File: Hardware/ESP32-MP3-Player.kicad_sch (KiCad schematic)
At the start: 17 parts, among them J1 Micro_SD_Card, J2 AudioJack3, J3 Battery, SW1 Reset, U1 ESP32-WROOM-32E, U2 MAX98357A, U3 AMS1117-3.3

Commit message: hardware: new analog circuit design
The old username is deprecated
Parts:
- removed C2, C3: 220pF, symbol Device:C
- removed FB1, FB2: FerriteBead, symbol Device:FerriteBead
- removed J2: AudioJack3, symbol Connector_Audio:AudioJack3
- added C10: 22uF, symbol Device:C
- added C11, C7, C9: 0.1uF, symbol Device:C
- added C6, C8: 10uF, symbol Device:C
- added J2: USB_C_Receptacle_USB2.0_14P, symbol Connector:USB_C_Receptacle_USB2.0_14P
- added J3: AudioJack3, symbol Connector_Audio:AudioJack3
- added J4: Debug, symbol Connector:Conn_01x04_Pin
- added R2: 210k, symbol Device:R
- added SW1: Power, symbol Switch:SW_SPDT
- added U3: MAX98357A, Package_DFN_QFN:TQFN-16-1EP_3x3mm_P0.5mm_EP1.23x1.23mm, symbol Audio:MAX98357A
- renumbered C6 to C1, C7 to C2, C1 to C3, J3 to J1, J1 to J5, SW1 to SW2, U3 to U1, U1 to U4
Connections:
- net +3V3: now also J5.4 (VDD), C10.1, C11.1, C6.1, C7.1, C8.1, C9.1, U3.7 (VDD), U3.8 (VDD)
- net +BATT: now also SW1.2 (B); no longer C1.1, U1.3 (VI)
- net BOOT: now also J4.1 (Pin_1)
- net GND: now also J5.6 (VSS), C10.2, C11.2, C6.2, C7.2, C8.2, C9.2, J2.A1 (GND), J2.A12 (GND), J2.B1 (GND), J2.B12 (GND), J2.S1 (SHIELD), J4.4 (Pin_4), U3.11 (GND), U3.15 (GND), U3.17 (PAD), U3.2 (GAIN_SLOT), U3.3 (GND)
- net at U2.9 (OUTP): now also J3.T
- net SD_DATA2: now reaches J5.1 (DAT2)
- net SD_DATA2: now also U4.14 (IO12)
- net SD_DATA3: now reaches J5.2 (DAT3/CD)
- net SD_DATA3: now also U4.16 (IO13)
- net SD_CMD: now reaches J5.3 (CMD)
- net SD_CMD: now also U4.23 (IO15)
- net SD_CLK: now reaches J5.5 (CLK)
- net SD_CLK: now also U4.13 (IO14)
- net SD_DATA0: now reaches J5.7 (DAT0)
- net SD_DATA0: now also U4.24 (IO2)
- net SD_DATA1: now reaches J5.8 (DAT1)
- net SD_DATA1: now also U4.26 (IO4)
- net at U2.10 (OUTN): now also J3.S, U3.10 (OUTN)
- net I2S_DIN: now reaches U2.1 (DIN)
- net I2S_DIN: now also U3.1 (DIN)
- net I2S_LRCLK: now reaches U2.14 (LRCLK)
- net I2S_LRCLK: now also U3.14 (LRCLK)
- net I2S_BCLK: now reaches U2.16 (BCLK)
- net I2S_BCLK: now also U3.16 (BCLK)
- net SD_MODE: now reaches U2.4 (~{SD_MODE})
- net SD_MODE: now also R2.2
- net RX0: now reaches U4.34 (RXD0/IO3)
- net RX0: now also J4.3 (Pin_3)
- net TX0: now reaches U4.35 (TXD0/IO1)
- net TX0: now also J4.2 (Pin_2)
- new net: J3.R, U3.9 (OUTP)
- new net: R2.1, U3.4 (~{SD_MODE})
- new net: C1.1, SW1.3 (C), U1.3 (VI)
- new net D+: J2.A6 (D+), J2.B6 (D+)
- new net D-: J2.A7 (D-), J2.B7 (D-)
- new net VBUS: J2.A4 (VBUS), J2.A9 (VBUS), J2.B4 (VBUS), J2.B9 (VBUS)
- no-connect marks 1 -> 3
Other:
- note added: "Debug"
- note added: "Ground"
- note added: "Left"
- note added: "Left Channel"
- note added: "MCU"
- note added: "Power"
- note added: "R_{SMALL} = 94.0 * V_{DDIO} - 100, in which V_{DDIO} stands for I/O voltage"
- note added: "Right"
- note added: "Right Channel"
- note added: "SD"
- note added: "TODO: charging circuit"
- note added: "TODO: improve analog audio circuit design"
- note added: "USB"
- note removed: "Two capacitors recommended in the datasheet"
- company: (none) -> Chubbyginger
- title: (none) -> ESP32-MP3-Player
- moved on the sheet: C1, C2, C3, J1, J5, R1, SW2, U1, U4

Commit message: hardware: Add OLED 12864
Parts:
- added C12, C13: 330pF, symbol Device:C
- added FB1: Ferrite Bead, symbol Device:FerriteBead_Small
- added FB2: FerriteBead_Small, symbol Device:FerriteBead_Small
- added J6: OLED 128x64, Display:OLED-128O064D, symbol Connector_Generic:Conn_01x04
- added R3: 0, symbol Device:R
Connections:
- net +BATT: now also C1.1, SW1.3 (C), U1.3 (VI), J6.2 (Pin_2); no longer J1.1 (Pin_1), SW1.2 (B)
- net GND: now also J6.1 (Pin_1), R3.2
- net at J3.R: now also FB2.2; no longer U3.9 (OUTP)
- net at J3.T: now also C12.1, FB1.2; no longer U2.9 (OUTP)
- new net: C12.2, C13.2, R3.1
- new net: FB1.1, U2.9 (OUTP)
- new net: C13.1, FB2.1, U3.9 (OUTP)
- new net: J1.1 (Pin_1), SW1.2 (B)
- new net OLED_SCL: J6.3 (Pin_3)
- new net OLED_SDA: J6.4 (Pin_4)
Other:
- note added: "OLED"
- moved on the sheet: J3

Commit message: hardware: digital circuit done!
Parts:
- added C1, C2: 100pF, symbol Device:C
- added R1, R2, R3, R4, R5: 10k, symbol Device:R
- added SW1: RotaryEncoder, symbol Device:RotaryEncoder_Switch
- added SW2: Back, symbol Switch:SW_Push
- added SW3: Hold, symbol Switch:SW_SPDT
- FB1: value Ferrite Bead -> FerriteBead_Small
- renumbered C7 to C10, C8 to C11, C11 to C12, C10 to C13, C3 to C14, C9 to C15, C1 to C3, C12 to C5, C5 to C6, C13 to C7, C2 to C8, C6 to C9, J2 to J1, J1 to J2, J6 to J4, J4 to J5, J5 to J6, R2 to R6, R3 to R7, R1 to R8, SW1 to SW4, SW2 to SW5, U2 to U1, U3 to U2, U1 to U3
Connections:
- net SD_MODE is gone; now on net AUD_SD_MODE: R6.2, U1.4 (~{SD_MODE})
- net +3V3: now also R1.1, R2.1, SW1.S1, SW2.2, SW3.2 (B)
- net GND: now also C1.2, C2.2, R3.2, R4.2, R5.2, SW1.C
- net I2S_BCLK: now also U4.12 (IO27)
- net I2S_DIN: now also U4.10 (IO25)
- net I2S_LRCLK: now also U4.11 (IO26)
- net OLED_SCL: now also U4.7 (IO35)
- net OLED_SDA: now also U4.6 (IO34)
- net AUD_SD_MODE: now reaches U4.29 (IO5)
- net SW_HOLD: now reaches U4.30 (IO18)
- net SW_HOLD: now also R5.1, SW3.3 (C)
- net ENC_DT: now reaches U4.31 (IO19)
- net ENC_DT: now also C1.1, R1.2, SW1.A
- net ENC_CLK: now reaches U4.33 (IO21)
- net ENC_CLK: now also C2.1, R2.2, SW1.B
- net ENC_SW: now reaches U4.36 (IO22)
- net ENC_SW: now also R3.1, SW1.S2
- net SW_BACK: now reaches U4.37 (IO23)
- net SW_BACK: now also R4.1, SW2.1
- no-connect marks 3 -> 10
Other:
- note added: "* GPIO16 and GPIO17 are occupied by internal PSRAM"
- note added: "Buttons"
- moved on the sheet: C10, C11, C12, C3, C4, C5, C6, C7, C8, C9, FB1, FB2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

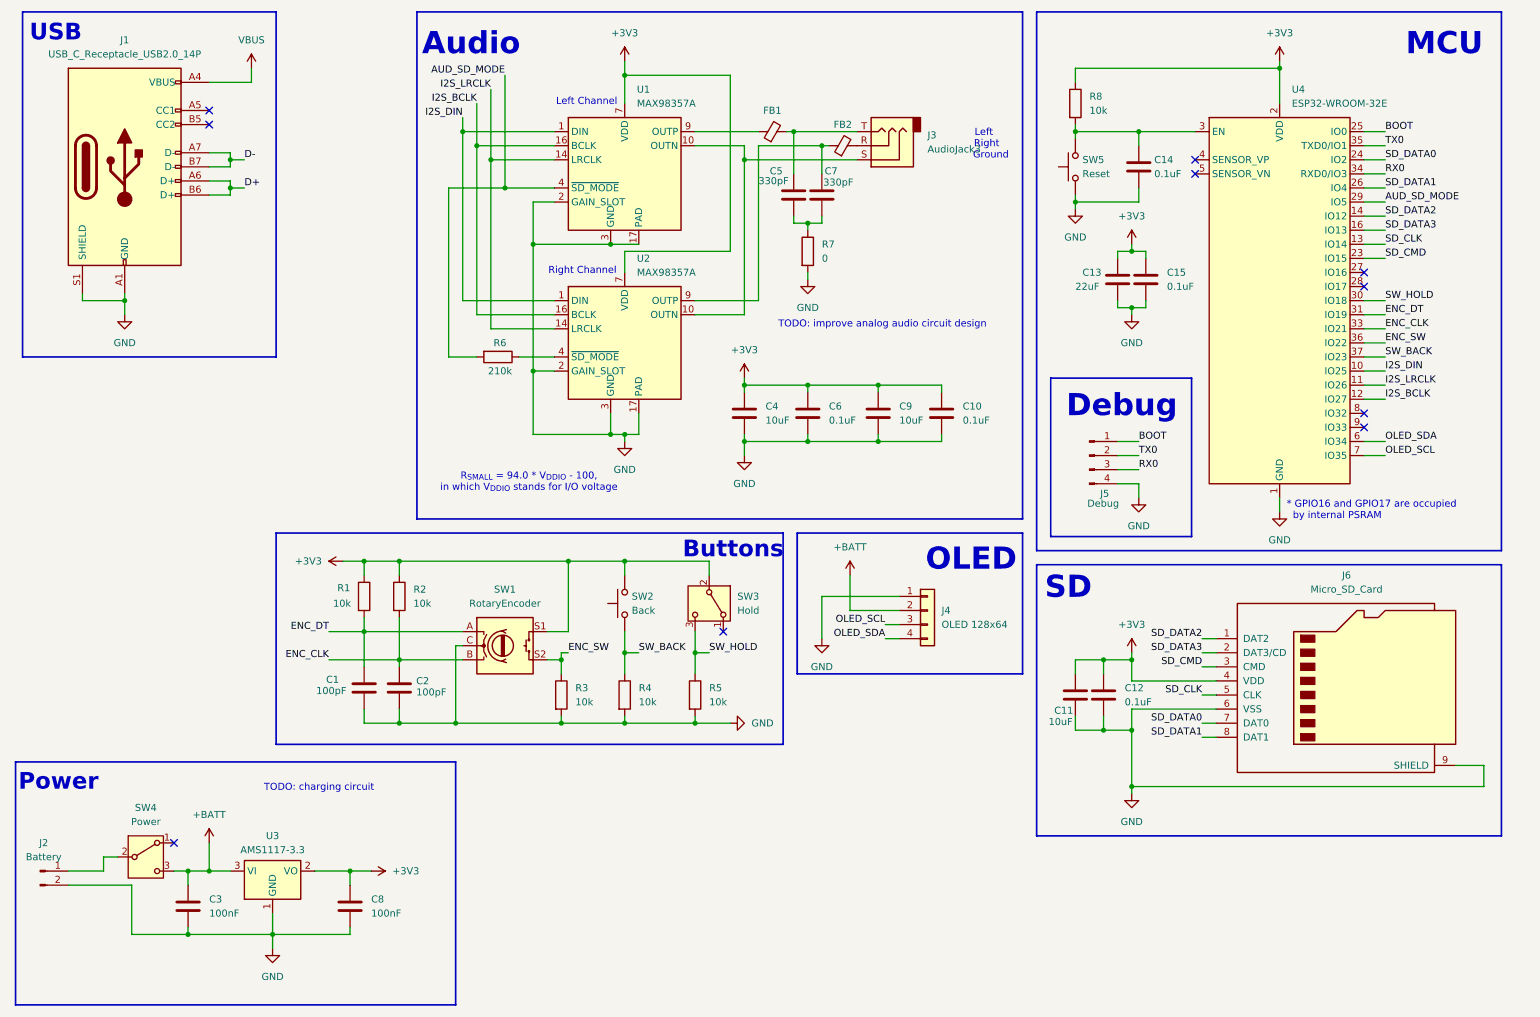
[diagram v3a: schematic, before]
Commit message: hardware: change i2c pin from 34,35 to 32,33
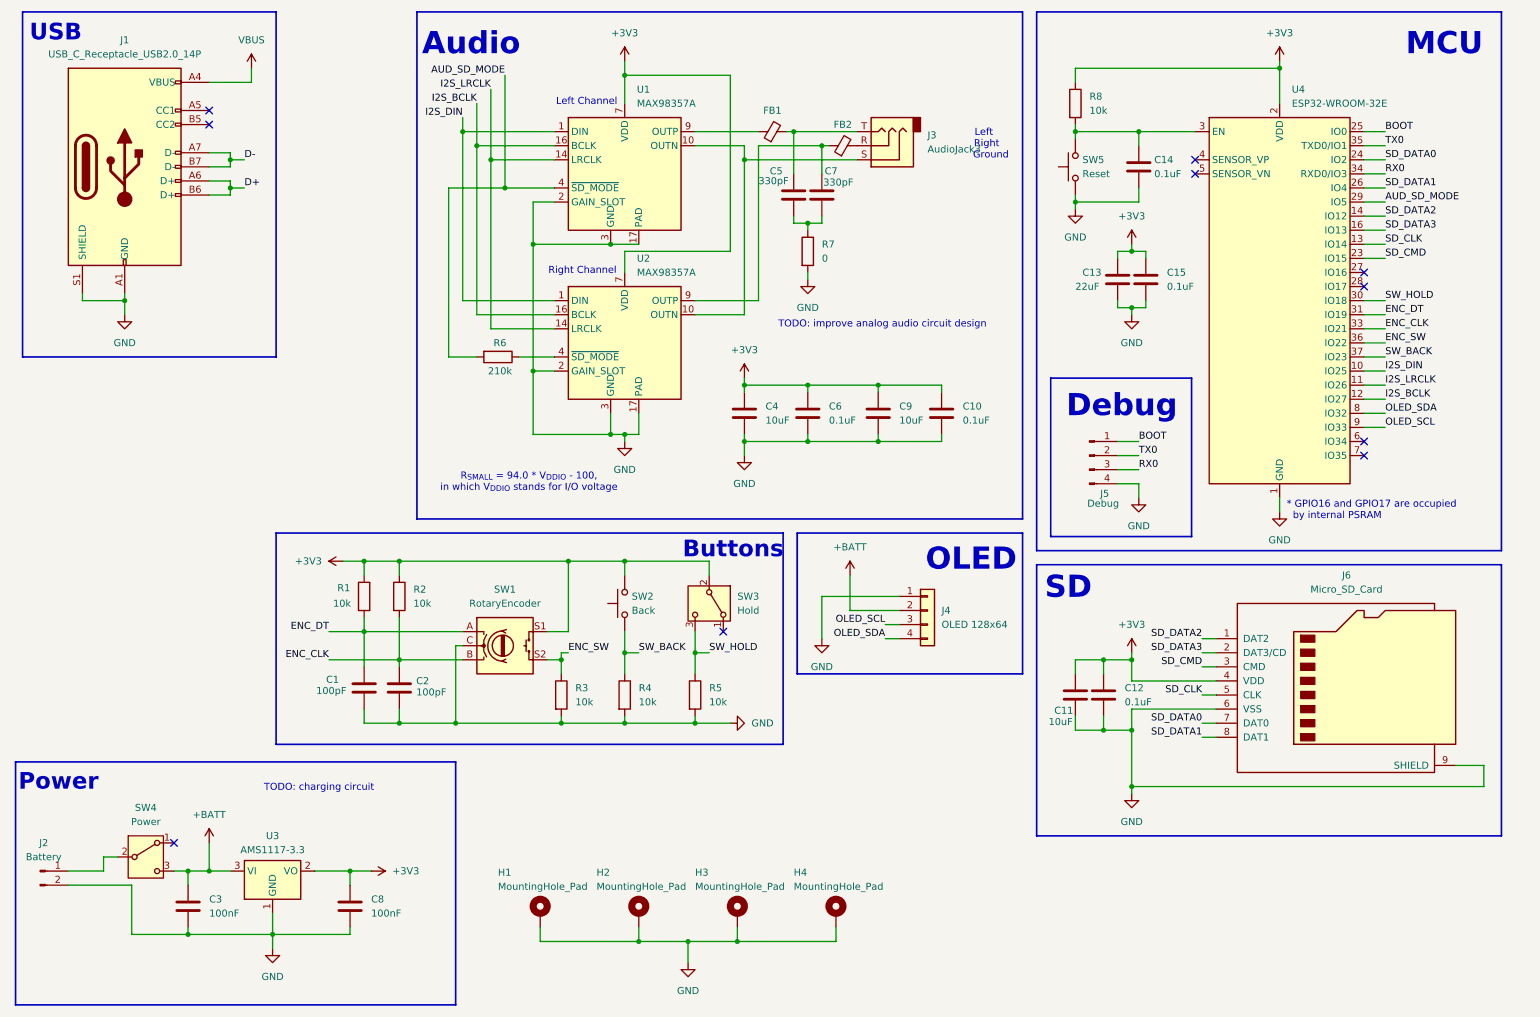
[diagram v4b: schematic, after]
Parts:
- added H1, H2, H3, H4: MountingHole_Pad, MountingHole:MountingHole_2.2mm_M2_DIN965_Pad, symbol Mechanical:MountingHole_Pad
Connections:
- net GND: now also H1.1, H2.1, H3.1, H4.1
- net OLED_SCL: now also U4.9 (IO33); no longer U4.7 (IO35)
- net OLED_SDA: now also U4.8 (IO32); no longer U4.6 (IO34)

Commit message: Hardware: add optional crystal
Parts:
- added C16, C17: 22pF, symbol Device:C
- added Y1: 32.768kHz, symbol Device:Crystal
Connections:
- net ENC_CLK: now also U4.31 (IO19); no longer U4.33 (IO21)
- net ENC_DT: now also U4.30 (IO18); no longer U4.31 (IO19)
- net ENC_SW: now also U4.33 (IO21); no longer U4.36 (IO22)
- net GND: now also C16.2, C17.2
- net OLED_SCL: now also U4.37 (IO23); no longer U4.9 (IO33)
- net OLED_SDA: now also U4.36 (IO22); no longer U4.8 (IO32)
- net SW_BACK: now also U4.7 (IO35); no longer U4.37 (IO23)
- net SW_HOLD: now also U4.6 (IO34); no longer U4.30 (IO18)
- new net 32CLK1: C16.1, U4.8 (IO32), Y1.1
- new net 32CLK2: C17.1, U4.9 (IO33), Y1.2
- no-connect marks 10 -> 8
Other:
- note added: "XTAL"
- note added: "reserved"
